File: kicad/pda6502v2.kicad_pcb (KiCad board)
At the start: 4 copper layers, 100 x 100 mm, 91 parts, among them J1 GPIO1, J2 GPIO2, J3 UART, J4 Screw_Terminal_01x02, J5 Conn_02x04_Odd_Even, J6 ICSP, J7 SPI, J8 FPGA_EXT, J9 SID, SW1 SW_Push, SW2 SW_Push, U1 W65C02SxP, U10 LT3030, U11 SC28L92A1B, U2 W65C22SxP, U3 W65C22SxP, U4 DS1818, U5 AS6C4008-55PCN, U6 ARMSID, U7 AT25M01, U8 ICE40HX4K-TQ144, U9 TLV1117-33, X1 8 MHz, X2 3.6864 MHz

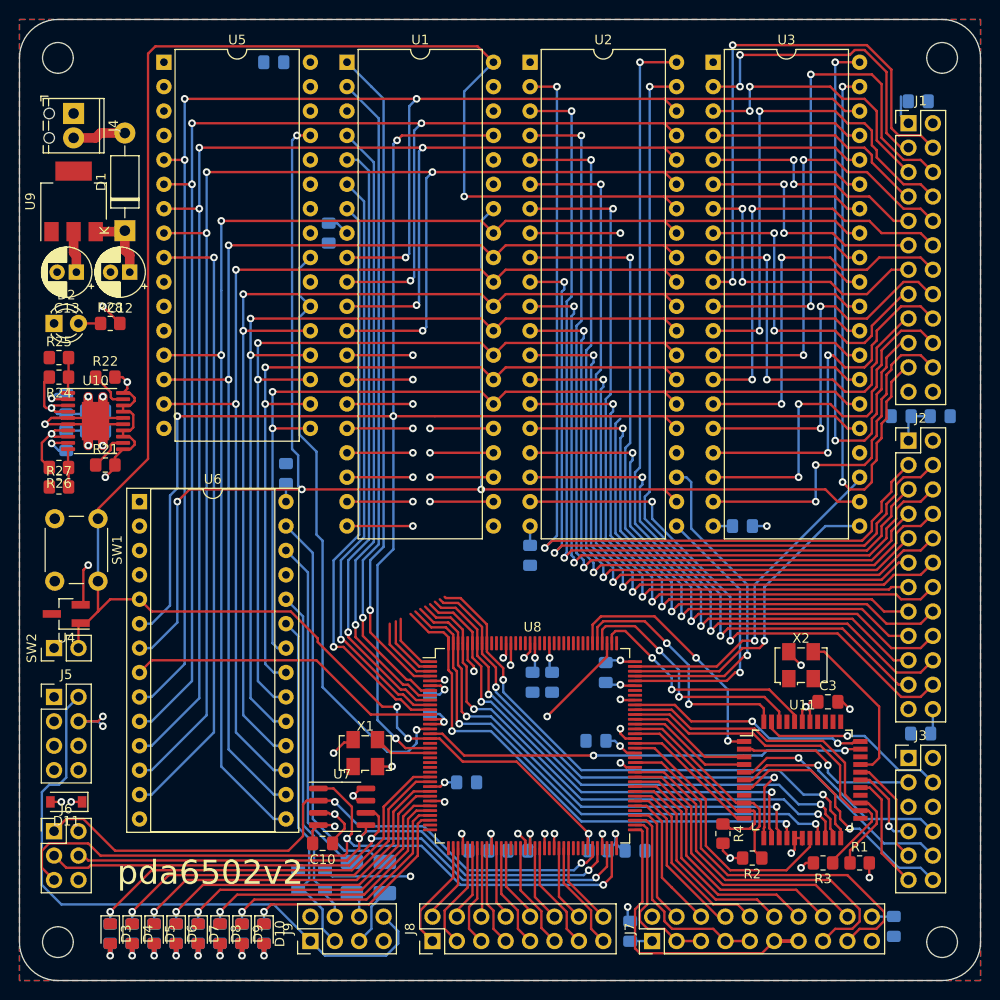
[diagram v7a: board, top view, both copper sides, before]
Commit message: More routing. D[0..7] etc.
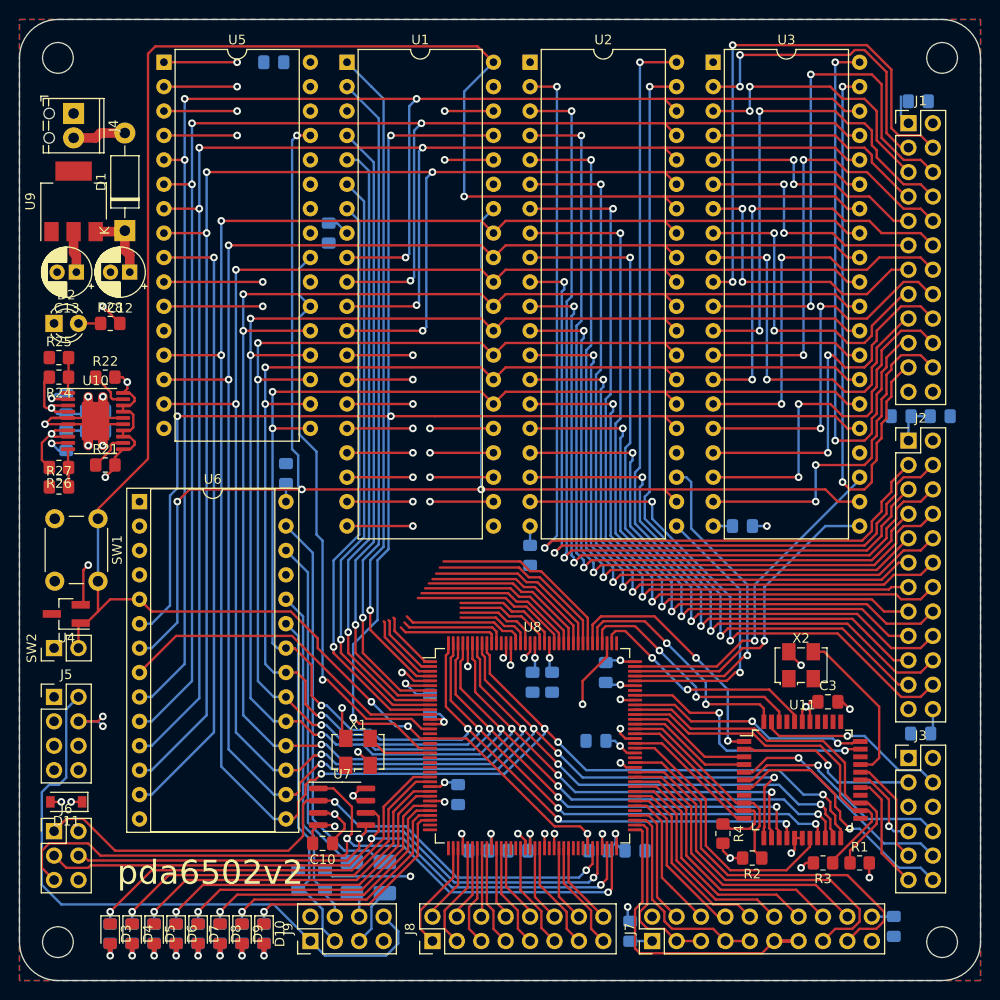
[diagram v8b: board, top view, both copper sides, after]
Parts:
- moved C16 1.55 mm to (143.6, 120.7), turned to 270 degrees
- moved X1 0.77 mm to (133.2, 116.2)
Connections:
- U8 pad 101: Net-(U8-Pad101) -> /RESET
- U8 pad 16: /RESET -> Net-(U8-Pad16)
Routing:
- net /A5: track 6.86 -> 36.7 mm, vias 1 -> 2
- net /A6: track 6.86 -> 36.2 mm, vias 1 -> 2
- net /D0: track 197.8 -> 222.4 mm, vias 4 -> 6
- net /D1: track 188.5 -> 210.9 mm, vias 4 -> 6
- net /A16: track 0.00 -> 20.6 mm, vias 0 -> 1
- net /D2: track 186.9 -> 207.4 mm, vias 4 -> 6
- net /A4: track 71.9 -> 92.0 mm
- net /GPIO2A6: track 57.7 -> 77.0 mm
- net /D6: track 160.7 -> 179.8 mm, vias 4 -> 6
- net /D7: track 151.3 -> 170.4 mm, vias 4 -> 6
- net /A12: track 6.60 -> 25.4 mm, vias 1 -> 2
- net /D3: track 176.4 -> 195.2 mm, vias 4 -> 6
- net /D4: track 174.0 -> 192.6 mm, vias 4 -> 6
- net /A7: track 6.86 -> 25.4 mm
- net /A18: track 0.00 -> 18.3 mm, vias 0 -> 1
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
